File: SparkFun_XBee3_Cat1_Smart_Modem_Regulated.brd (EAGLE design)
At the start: 35.6 x 52.1 mm, 97 parts, among them J4 QWIIC_RIGHT_ANGLE, U2 AP63203

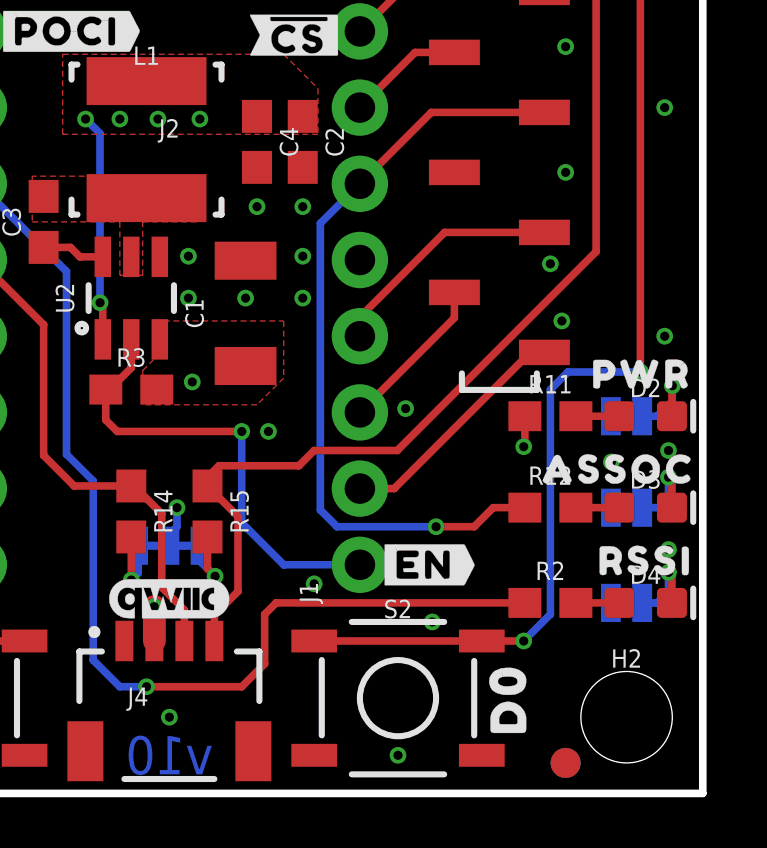
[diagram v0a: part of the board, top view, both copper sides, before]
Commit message: Moves LEDs around for consistency with the development board
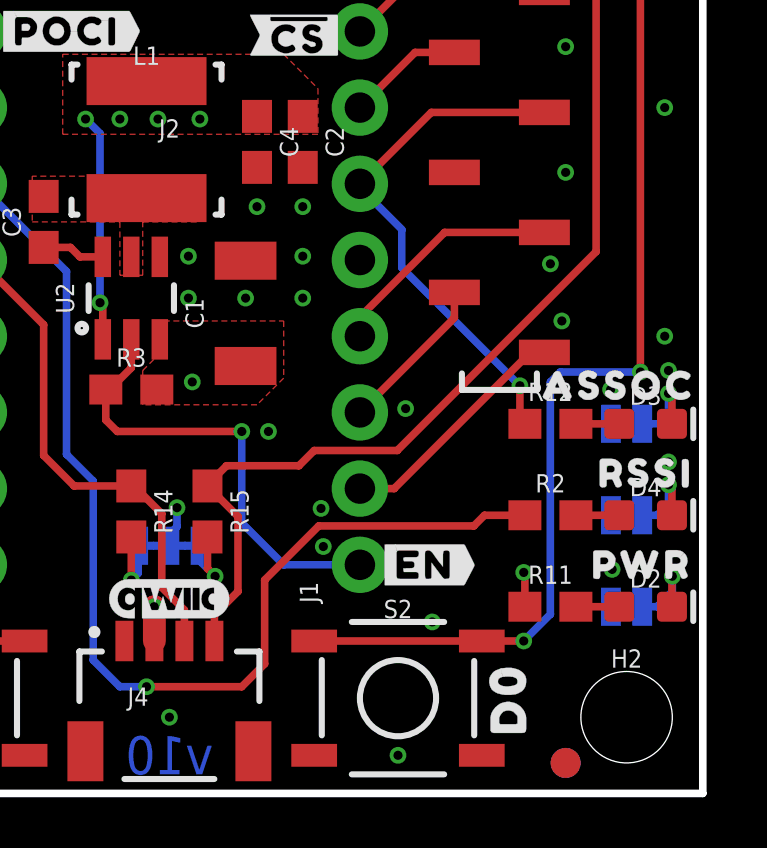
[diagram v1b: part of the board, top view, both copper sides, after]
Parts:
- moved D2 6.35 mm to (32.4, 6.22)
- moved PLED 6.35 mm to (31.8, 6.22)
- moved R11 6.35 mm to (29.2, 6.22)
- moved U$42 6.35 mm to (32.3, 7.62)
- moved U$52 6.35 mm to (28.3, 6.22)
- moved D4 2.92 mm to (32.4, 9.27)
- moved R2 2.92 mm to (29.2, 9.27)
- moved RLED 2.92 mm to (31.8, 9.27)
- moved U$11 2.92 mm to (28.3, 9.27)
- moved U$62 2.92 mm to (32.4, 10.7)
- moved ALED 2.79 mm to (31.8, 12.3)
- moved D3 2.79 mm to (32.4, 12.3)
- moved R12 2.79 mm to (29.2, 12.3)
- moved U$43 2.79 mm to (31.5, 13.6)
- moved U$49 2.79 mm to (28.2, 12.4)
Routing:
- net D5/ASSOCIATE: track 25.9 -> 17.5 mm
- net D10/RSSI_PWM: track 38.5 -> 40.4 mm
- net GND: vias 38 -> 40
